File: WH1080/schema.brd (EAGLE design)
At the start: 78.4 x 80 mm, 18 parts

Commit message: +
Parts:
- removed ANEMO, RAIN: XRJK-S-01-6-4-0-9M2, con-xmultiple:XRJK-S-01-6-4-0-9M2
- added J1, J2: RJ11, SparkFun-Connectors:RJ11-6
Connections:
- net GND: now also J1.3, J2.2, J2.3; no longer ANEMO.1, ANEMO.2, RAIN.2
- net N$1: now also J1.4; no longer RAIN.3
- net N$2: now also J2.5; no longer ANEMO.4
- net N$4: now also J2.4; no longer ANEMO.3
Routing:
- net N$1: track 25.5 -> 28.1 mm
- net N$2: track 28.6 -> 31.2 mm
- net GND: track 160.2 -> 159.3 mm

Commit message: +
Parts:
- removed J1, J2: RJ11, SparkFun-Connectors:RJ11-6
- added RAIN, WIND: RJ11-4, pf:RJ11-4
- moved C1 10.2 mm to (25.4, 52.1)
- moved C2 10.2 mm to (25.4, 55.9)
- moved C3 10.2 mm to (31.8, 55.9)
- moved R2 10.2 mm to (25.4, 44.5)
- moved R3 10.2 mm to (25.4, 47.0)
- moved R4 10.2 mm to (25.4, 49.5)
- moved WEMOS3 10.2 mm to (26.7, 49.5)
- moved CON->RAD 10.2 mm to (45.7, 76.2)
- moved CON1 10.2 mm to (11.4, 76.2)
- moved R1 10.2 mm to (29.2, 77.5)
- moved HUMIDITY 1.27 mm to (67.3, 41.9)
- moved PRESSURE 1.27 mm to (67.3, 48.3)
- moved TEMPERATURE 1.27 mm to (69.8, 15.2)
- moved CON->MAIN 1.27 mm to (68.6, 22.9)
- moved SL4 1.27 mm to (67.3, 29.2)
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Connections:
- net GND: now also RAIN.2, WIND.1, WIND.5; no longer J1.3, J2.2, J2.3
- net N$1: now also RAIN.5; no longer J1.4
- net N$2: now also WIND.6; no longer J2.5
- net N$4: now also WIND.2; no longer J2.4
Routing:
- net N$6: track 80.0 -> 97.8 mm
- net GND: track 159.3 -> 171.8 mm
- net N$2: track 31.2 -> 36.1 mm
- net N$1: track 28.1 -> 31.2 mm
- net +3V3: track 166.7 -> 163.7 mm
- net N$4: track 34.8 -> 35.3 mm
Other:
- board size 78.4 x 80 mm -> 78.4 x 97.8 mm

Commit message: +
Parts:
- removed WEMOS3: (no value), esp8266modules:WEMOS-D1-MINI
- added R5: 4k7, rcl:0204/7
- added U$1: WEMOS_S2_MINI, Wemos_Boards:S2_MINI
- moved R1 34.5 mm to (25.4, 43.2), turned to 0 degrees
- moved C1 9.92 mm to (33.0, 45.7)
- moved C2 9.16 mm to (33.0, 50.8)
- moved R4 3.81 mm to (25.4, 53.3)
- moved R3 3.81 mm to (25.4, 50.8)
- moved C3 2.84 mm to (33.0, 53.3)
- moved R2 1.27 mm to (25.4, 45.7)
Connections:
- removed net +5V: WEMOS3.5V
- removed net N$3: CON->RAD.B5, CON1.B2, R1.1, WEMOS3.D4
- removed net N$5: CON->RAD.B3, CON1.B4, WEMOS3.D1
- removed net N$7: CON->RAD.B4, CON1.B3, WEMOS3.D2
- new net GND2: U$1.P22
- new net N$10: CON->MAIN.1, HUMIDITY.1, PRESSURE.1, SL3.1, SL4.1
- new net N$11: CON->MAIN.2, HUMIDITY.2, PRESSURE.2, SL3.2, SL4.2
- new net N$12: U$1.P0
- new net N$13: CON1.B1, R1.2, U$1.P1
- new net N$14: CON->RAD.B1, U$1.P5
- new net N$15: U$1.P9
- new net N$16: U$1.P10
- new net N$17: U$1.P11
- new net VBUS: U$1.P7
- net +3V3: now also CON->RAD.B2, CON1.B2, R1.1, R5.1, U$1.P8; no longer CON->RAD.B1, CON1.B6, R1.2, WEMOS3.3V3
- net GND: now also CON->RAD.B3, CON1.B3, U$1.P6; no longer CON->RAD.B6, CON1.B1, WEMOS3.GND
- net N$1: now also U$1.P13; no longer WEMOS3.D8
- net N$2: now also U$1.P12; no longer WEMOS3.A0
- net N$4: now also U$1.P14; no longer WEMOS3.D7
- net N$9: now also R5.2
- net SCL: now also CON->RAD.B5, CON1.B5, U$1.P2; no longer CON->MAIN.2, HUMIDITY.2, PRESSURE.2, SL3.2, SL4.2
- net SDA: now also CON->RAD.B4, CON1.B4, U$1.P3; no longer CON->MAIN.1, HUMIDITY.1, PRESSURE.1, SL3.1, SL4.1
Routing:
- net +3V3: track 163.7 -> 28.0 mm
- net GND: track 171.8 -> 90.0 mm
- net N$7: track 45.4 -> 0.00 mm
- net N$5: track 42.9 -> 0.00 mm
- net N$3: track 41.8 -> 0.00 mm
- net N$2: track 36.1 -> 0.00 mm
- net N$4: track 35.3 -> 0.00 mm
- net N$1: track 31.2 -> 0.00 mm
- net N$10: track 0.00 -> 25.6 mm
- net SDA: track 25.6 -> 0.14 mm
- net SCL: track 25.4 -> 0.00 mm
- net N$11: track 0.00 -> 25.4 mm

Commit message: vyroba DPS
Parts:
- added SL1: (no value), con-amp-quick:02P
- added SL5: (no value), con-amp-quick:04P
- U$1: value WEMOS_S2_MINI -> WEMOS-D1-MINI; device Wemos_Boards:S2_MINI -> Wemos_Boards:WEMOS-D1-MINI
- moved R5 51.1 mm to (67.3, 19.1)
- moved U$1 22.2 mm to (27.9, 49.5)
- moved CON->MAIN 8.89 mm to (68.6, 14.0)
- moved TEMPERATURE 8.03 mm to (67.3, 22.9)
- moved CON1 6.35 mm to (17.8, 76.2), turned to 270 degrees
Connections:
- removed net GND2: U$1.P22
- removed net N$1: C1.1, R2.2, RAIN.5, U$1.P13
- removed net N$12: U$1.P0
- removed net N$15: U$1.P9
- removed net N$16: U$1.P10
- removed net N$17: U$1.P11
- removed net N$2: C3.1, R4.2, U$1.P12, WIND.6
- removed net N$4: C2.1, R3.2, U$1.P14, WIND.2
- removed net VBUS: U$1.P7
- new net 5V: U$1.JP2.8
- new net GND1: CON->MAIN.3, HUMIDITY.3, PRESSURE.3, SL3.3, SL4.3, TEMPERATURE.1
- new net PULS: C1.1, R2.2, RAIN.3, SL1.1, U$1.JP1.7
- new net RYCHLOST: C2.1, R3.2, SL5.2, U$1.JP1.6, WIND.3
- new net SMER: C3.1, R4.2, SL5.1, U$1.JP1.2, WIND.4
- new net VCC: CON->MAIN.4, HUMIDITY.4, PRESSURE.4, R5.1, SL3.4, SL4.4, TEMPERATURE.3
- net +3V3: now also U$1.JP1.8; no longer CON->MAIN.4, HUMIDITY.4, PRESSURE.4, R5.1, SL3.4, SL4.4, TEMPERATURE.3, U$1.P8
- net GND: now also SL1.2, SL5.3, SL5.4, U$1.JP2.7, WIND.2; no longer CON->MAIN.3, HUMIDITY.3, PRESSURE.3, SL3.3, SL4.3, TEMPERATURE.1, U$1.P6, WIND.5
- net N$13: now also U$1.JP2.5; no longer U$1.P1
- net N$14: now also U$1.JP2.6; no longer U$1.P5
- net SCL: now also U$1.JP2.3; no longer U$1.P2
- net SDA: now also U$1.JP2.4; no longer U$1.P3
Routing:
- net N$6: track 97.8 -> 0.00 mm
- net SCL: track 0.00 -> 71.0 mm, vias 0 -> 1
- net SDA: track 0.14 -> 69.7 mm
- net SMER: track 0.00 -> 57.6 mm
- net N$13: track 0.00 -> 57.3 mm
- net N$14: track 0.00 -> 55.3 mm
- net RYCHLOST: track 0.00 -> 53.3 mm
- net PULS: track 0.00 -> 51.7 mm
- net GND: track 90.0 -> 141.5 mm
- net VCC: track 0.00 -> 42.6 mm
- net +3V3: track 28.0 -> 66.2 mm
- net GND1: track 0.00 -> 36.5 mm
- net N$11: track 25.4 -> 35.1 mm
- net N$10: track 25.6 -> 35.2 mm
- net N$9: track 7.33 -> 13.5 mm

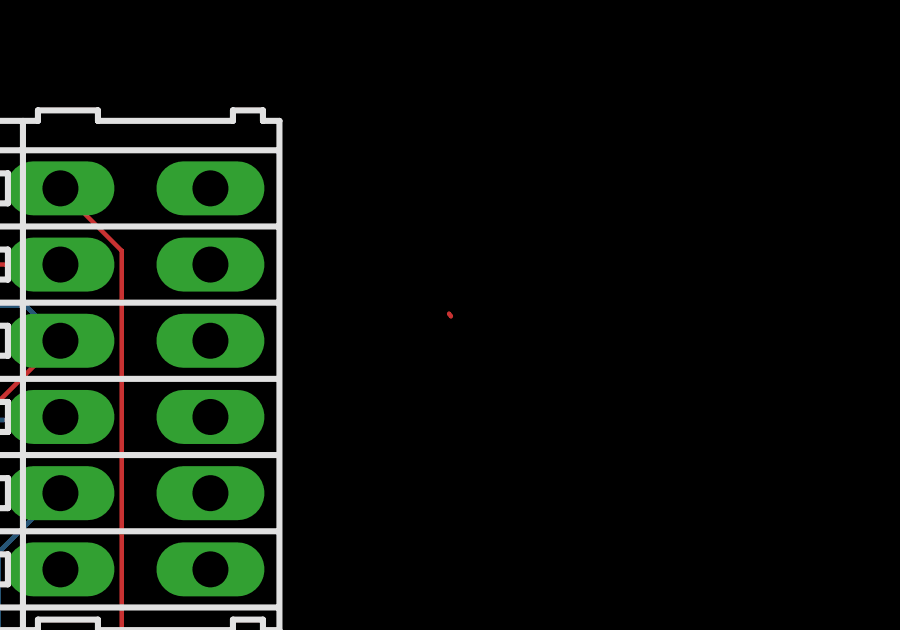
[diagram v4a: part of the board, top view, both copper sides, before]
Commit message: změna odporu pro dělič směru větru
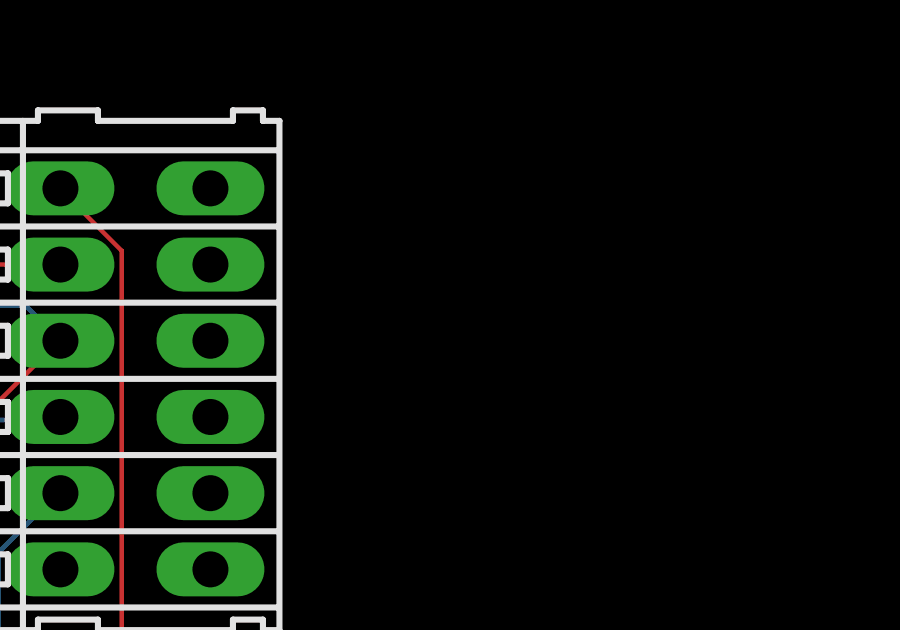
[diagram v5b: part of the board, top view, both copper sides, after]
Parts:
- C1: value 100n -> 10p
- C2: value 100n -> 100p
- R4: value 10k -> 47k
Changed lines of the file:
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@@
 </autorouter>
 <elements>
-<element name="C1" library="rcl" library_urn="urn:adsk.eagle:library:334" package="C025-024X044" package3d_urn="urn:adsk.eagle:package:23630/1" value="100n" x="33.02" y="45.72" smashed="yes">
+<element name="C1" library="rcl" library_urn="urn:adsk.eagle:library:334" package="C025-024X044" package3d_urn="urn:adsk.eagle:package:23630/1" value="10p" x="33.02" y="45.72" smashed="yes">
 <attribute name="NAME" x="31.242" y="43.307" size="1.27" layer="25" ratio="10"/>
 <attribute name="POPULARITY" value="56" x="73.66" y="-17.78" size="1.778" layer="27" display="off"/>
@@
 <attribute name="VALUE" x="36.957" y="42.672" size="1.27" layer="27" ratio="10" rot="R90"/>
 </element>
-<element name="C2" library="rcl" library_urn="urn:adsk.eagle:library:334" package="C025-024X044" package3d_urn="urn:adsk.eagle:package:23630/1" value="100n" x="33.02" y="50.8" smashed="yes">
+<element name="C2" library="rcl" library_urn="urn:adsk.eagle:library:334" package="C025-024X044" package3d_urn="urn:adsk.eagle:package:23630/1" value="100p" x="33.02" y="50.8" smashed="yes">
 <attribute name="NAME" x="31.242" y="52.197" size="1.27" layer="25" ratio="10"/>
 <attribute name="POPULARITY" value="56" x="78.74" y="-12.7" size="1.778" layer="27" display="off"/>
@@
 <attribute name="VALUE" x="62.484" y="10.1346" size="1.27" layer="27" ratio="10"/>
 </element>
-<element name="R4" library="rcl" library_urn="urn:adsk.eagle:library:334" package="0204/7" package3d_urn="urn:adsk.eagle:package:23498/2" value="10k" x="25.4" y="53.34" smashed="yes">
+<element name="R4" library="rcl" library_urn="urn:adsk.eagle:library:334" package="0204/7" package3d_urn="urn:adsk.eagle:package:23498/2" value="47k" x="25.4" y="53.34" smashed="yes">
 <attribute name="NAME" x="22.86" y="54.6354" size="0.9906" layer="25" ratio="10"/>
 <attribute name="POPULARITY" value="79" x="25.4" y="53.34" size="1.778" layer="27" display="off"/>
@@
 <wire x1="43.1292" y1="74.8284" x2="43.22" y2="74.93" width="0.1524" layer="16"/>
 </signal>
-<signal name="VDD">
-<wire x1="56.2356" y1="78.2828" x2="56.175" y2="78.375" width="0.1524" layer="1"/>
-</signal>
 <signal name="N$9">

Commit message: +
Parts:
- R2: value 100k -> 10k
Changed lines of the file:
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@@
 <attribute name="VALUE" x="23.03" y="75.94" size="1.27" layer="27" rot="R270"/>
 </element>
-<element name="R2" library="rcl" library_urn="urn:adsk.eagle:library:334" package="0204/7" package3d_urn="urn:adsk.eagle:package:23498/2" value="100k" x="25.4" y="45.72" smashed="yes">
+<element name="R2" library="rcl" library_urn="urn:adsk.eagle:library:334" package="0204/7" package3d_urn="urn:adsk.eagle:package:23498/2" value="10k" x="25.4" y="45.72" smashed="yes">
 <attribute name="NAME" x="19.05" y="45.7454" size="0.9906" layer="25" ratio="10"/>
 <attribute name="POPULARITY" value="79" x="43.18" y="-30.48" size="1.778" layer="27" display="off"/>
